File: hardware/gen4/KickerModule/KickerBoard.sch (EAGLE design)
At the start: 106 parts

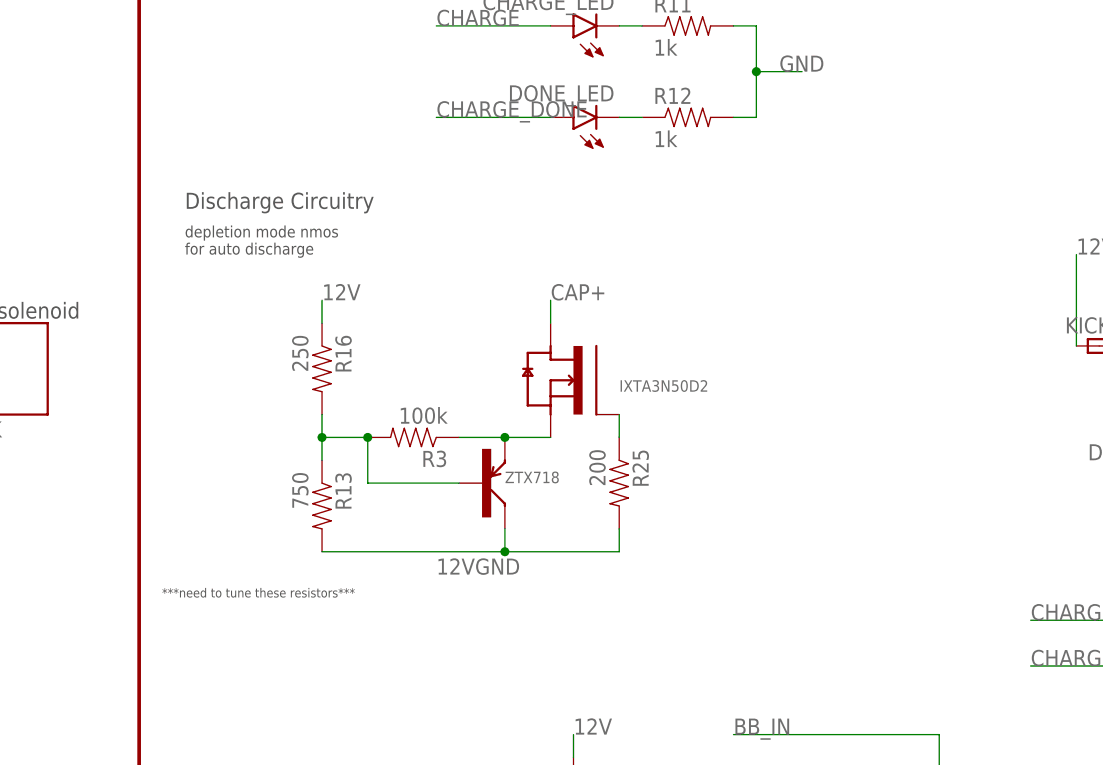
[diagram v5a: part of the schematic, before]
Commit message: discharge circuit improved in schematic
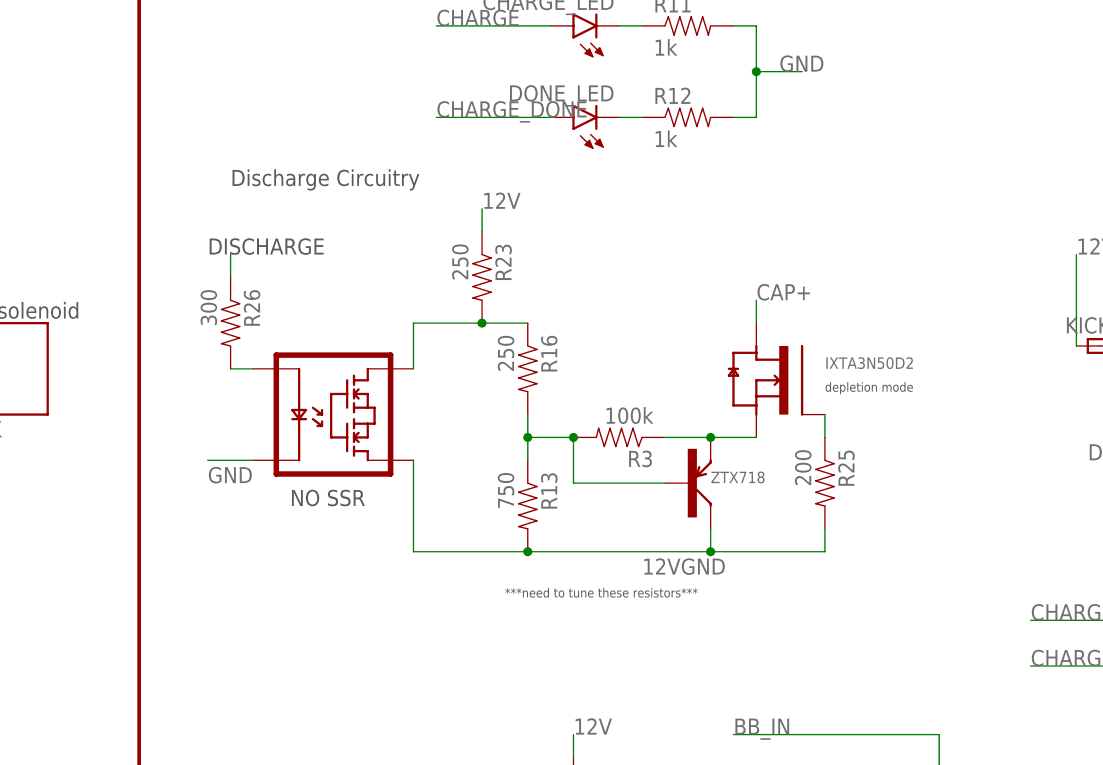
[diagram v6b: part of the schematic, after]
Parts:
- added R23: 250, SparkFun-Passives:RESISTOR0805-RES
- added R26: 300, SparkFun-Passives:RESISTOR0805-RES
- added U$5: VO1400AEFTR, rfc:VO1400AEFTR
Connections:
- new net N$29: R16.1, R23.2, U$5.S1
- new net N$30: R26.2, U$5.LED+
- net 12V: now also R23.1; no longer R16.1
- net 12VGND: now also U$5.S2
- net DISCHARGE: now also R26.1
- net GND: now also U$5.LED-
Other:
- note added: "NO SSR"
- note added: "depletion mode"
- note removed: "depletion mode nmos for auto discharge"
- moved on the sheet: R13, R16, R25, R3
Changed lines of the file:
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@@
 <part name="R16" library="SparkFun-Passives" deviceset="RESISTOR" device="0805-RES" value="250"/>
 <part name="R25" library="SparkFun-Passives" deviceset="RESISTOR" device="0805-RES" value="200"/>
+<part name="U$5" library="rfc" deviceset="VO1400AEFTR" device=""/>
+<part name="R23" library="SparkFun-Passives" deviceset="RESISTOR" device="0805-RES" value="250"/>
+<part name="R26" library="SparkFun-Passives" deviceset="RESISTOR" device="0805-RES" value="300"/>
 </parts>
 <sheets>
@@
 <text x="444.5" y="261.62" size="1.778" layer="97">threshold = 50% of xref</text>
 <text x="698.5" y="370.84" size="1.778" layer="97">same radius, but shorter than old caps</text>
-<text x="513.08" y="350.52" size="1.778" layer="97">Discharge Circuitry</text>
+<text x="518.16" y="353.06" size="1.778" layer="97">Discharge Circuitry</text>
 <text x="538.48" y="241.3" size="1.778" layer="97">capacitor sense circuitry</text>
 <text x="553.72" y="256.54" size="1.778" layer="97" rot="R180">15v -&gt; 3v division
@@
 1.3v drop, 100mA.
 2V / 20 ohm = 100mA</text>
-<text x="513.08" y="345.44" size="1.27" layer="97">depletion mode nmos
-for auto discharge</text>
 <text x="492.252" y="338.328" size="1.778" layer="97">solenoid</text>
 <text x="493.014" y="279.908" size="1.778" layer="97">solenoid</text>
 <text x="386.08" y="231.14" size="1.778" layer="97">DISCHARGE</text>
-<text x="561.34" y="330.2" size="1.27" layer="95">IXTA3N50D2</text>
-<text x="548.64" y="320.04" size="1.27" layer="95">ZTX718</text>
-<text x="510.54" y="307.34" size="1.016" layer="97">***need to tune these resistors***</text>
+<text x="584.2" y="332.74" size="1.27" layer="95">IXTA3N50D2</text>
+<text x="571.5" y="320.04" size="1.27" layer="95">ZTX718</text>
+<text x="548.64" y="307.34" size="1.016" layer="97">***need to tune these resistors***</text>
+<text x="584.2" y="330.2" size="1.016" layer="97">depletion mode</text>
+<text x="515.62" y="345.44" size="1.778" layer="97">DISCHARGE</text>
+<text x="524.764" y="317.5" size="1.778" layer="97">NO SSR</text>
 </plain>
 <instances>
@@
 <attribute name="VALUE" x="613.41" y="332.359" size="1.778" layer="96"/>
 </instance>
-<instance part="U$2" gate="G$1" x="558.8" y="327.66" rot="MR0"/>
-<instance part="U$6" gate="G$1" x="546.1" y="314.96"/>
-<instance part="R3" gate="G$1" x="538.48" y="325.12" rot="R180"/>
-<instance part="R13" gate="G$1" x="528.32" y="317.5" rot="R270"/>
-<instance part="R16" gate="G$1" x="528.32" y="332.74" rot="R270"/>
-<instance part="R25" gate="G$1" x="561.34" y="320.04" rot="R270"/>
+<instance part="U$2" gate="G$1" x="581.66" y="327.66" rot="MR0"/>
+<instance part="U$6" gate="G$1" x="568.96" y="314.96"/>
+<instance part="R3" gate="G$1" x="561.34" y="325.12" rot="R180"/>
+<instance part="R13" gate="G$1" x="551.18" y="317.5" rot="R270"/>
+<instance part="R16" gate="G$1" x="551.18" y="332.74" rot="R270"/>
+<instance part="R25" gate="G$1" x="584.2" y="320.04" rot="R270"/>
+<instance part="U$5" gate="G$1" x="520.7" y="325.12"/>
+<instance part="R23" gate="G$1" x="546.1" y="342.9" rot="R270"/>
+<instance part="R26" gate="G$1" x="518.16" y="337.82" rot="R270"/>
 </instances>
 <busses>
@@
 <junction x="368.3" y="208.28"/>
 <wire x1="368.3" y1="208.28" x2="383.54" y2="208.28" width="0.1524" layer="91"/>
+<label x="515.62" y="320.04" size="1.778" layer="95"/>
+</segment>
+<segment>
+<pinref part="U$5" gate="G$1" pin="LED-"/>
+<wire x1="520.7" y1="322.58" x2="515.62" y2="322.58" width="0.1524" layer="91"/>
 </segment>
 </net>
@@
 <wire x1="482.6" y1="307.34" x2="482.6" y2="302.26" width="0.1524" layer="91"/>
 <label x="482.6" y="302.26" size="1.778" layer="95"/>
-<label x="541.02" y="309.88" size="1.778" layer="95"/>
+<label x="563.88" y="309.88" size="1.778" layer="95"/>
 </segment>
 <segment>
@@
 <pinref part="U$6" gate="G$1" pin="COLLECTOR"/>
 <pinref part="R13" gate="G$1" pin="2"/>
-<wire x1="548.64" y1="314.96" x2="548.64" y2="312.42" width="0.1524" layer="91"/>
-<wire x1="548.64" y1="312.42" x2="528.32" y2="312.42" width="0.1524" layer="91"/>
+<wire x1="571.5" y1="314.96" x2="571.5" y2="312.42" width="0.1524" layer="91"/>
+<wire x1="571.5" y1="312.42" x2="551.18" y2="312.42" width="0.1524" layer="91"/>
 <pinref part="R25" gate="G$1" pin="2"/>
-<wire x1="548.64" y1="312.42" x2="561.34" y2="312.42" width="0.1524" layer="91"/>
-<wire x1="561.34" y1="312.42" x2="561.34" y2="314.96" width="0.1524" layer="91"/>
-<junction x="548.64" y="312.42"/>
+<wire x1="571.5" y1="312.42" x2="584.2" y2="312.42" width="0.1524" layer="91"/>
+<wire x1="584.2" y1="312.42" x2="584.2" y2="314.96" width="0.1524" layer="91"/>
+<junction x="571.5" y="312.42"/>
+<pinref part="U$5" gate="G$1" pin="S2"/>
+<wire x1="538.48" y1="322.58" x2="538.48" y2="312.42" width="0.1524" layer="91"/>
+<wire x1="538.48" y1="312.42" x2="551.18" y2="312.42" width="0.1524" layer="91"/>
+<junction x="551.18" y="312.42"/>
 </segment>
 </net>
@@
 </segment>
 <segment>
-<label x="553.72" y="340.36" size="1.778" layer="95"/>
-<wire x1="553.72" y1="337.82" x2="553.72" y2="340.36" width="0.1524" layer="91"/>
+<label x="576.58" y="340.36" size="1.778" layer="95"/>
+<wire x1="576.58" y1="337.82" x2="576.58" y2="340.36" width="0.1524" layer="91"/>
 <pinref part="U$2" gate="G$1" pin="DRAIN"/>
 </segment>
@@
 <wire x1="612.14" y1="335.28" x2="612.14" y2="345.44" width="0.1524" layer="91"/>
 <label x="612.14" y="345.44" size="1.778" layer="95"/>
-<label x="528.32" y="340.36" size="1.778" layer="95"/>
-</segment>
-<segment>
-<pinref part="R16" gate="G$1" pin="1"/>
-<wire x1="528.32" y1="337.82" x2="528.32" y2="340.36" width="0.1524" layer="91"/>
+<label x="546.1" y="350.52" size="1.778" layer="95"/>
+</segment>
+<segment>
+<pinref part="R23" gate="G$1" pin="1"/>
+<wire x1="546.1" y1="347.98" x2="546.1" y2="350.52" width="0.1524" layer="91"/>
 </segment>
 </net>
@@
 <wire x1="383.54" y1="231.14" x2="393.7" y2="231.14" width="0.1524" layer="91"/>
 <junction x="383.54" y="231.14"/>
+</segment>
+<segment>
+<pinref part="R26" gate="G$1" pin="1"/>
+<wire x1="518.16" y1="342.9" x2="518.16" y2="345.44" width="0.1524" layer="91"/>
 </segment>
 </net>
@@
 <pinref part="U$2" gate="G$1" pin="SOURCE"/>
 <pinref part="U$6" gate="G$1" pin="EMITTER"/>
-<wire x1="553.72" y1="325.12" x2="548.64" y2="325.12" width="0.1524" layer="91"/>
+<wire x1="576.58" y1="325.12" x2="571.5" y2="325.12" width="0.1524" layer="91"/>
 <pinref part="R3" gate="G$1" pin="1"/>
-<wire x1="548.64" y1="325.12" x2="543.56" y2="325.12" width="0.1524" layer="91"/>
-<junction x="548.64" y="325.12"/>
+<wire x1="571.5" y1="325.12" x2="566.42" y2="325.12" width="0.1524" layer="91"/>
+<junction x="571.5" y="325.12"/>
 </segment>
 </net>
@@
 <pinref part="R16" gate="G$1" pin="2"/>
 <pinref part="R13" gate="G$1" pin="1"/>
-<wire x1="528.32" y1="327.66" x2="528.32" y2="325.12" width="0.1524" layer="91"/>
+<wire x1="551.18" y1="327.66" x2="551.18" y2="325.12" width="0.1524" layer="91"/>
 <pinref part="R3" gate="G$1" pin="2"/>
-<wire x1="528.32" y1="325.12" x2="528.32" y2="322.58" width="0.1524" layer="91"/>
-<wire x1="533.4" y1="325.12" x2="528.32" y2="325.12" width="0.1524" layer="91"/>
-<junction x="528.32" y="325.12"/>
+<wire x1="551.18" y1="325.12" x2="551.18" y2="322.58" width="0.1524" layer="91"/>
+<wire x1="556.26" y1="325.12" x2="551.18" y2="325.12" width="0.1524" layer="91"/>
+<junction x="551.18" y="325.12"/>
 <pinref part="U$6" gate="G$1" pin="BASE"/>
-<wire x1="543.56" y1="320.04" x2="533.4" y2="320.04" width="0.1524" layer="91"/>
-<wire x1="533.4" y1="320.04" x2="533.4" y2="325.12" width="0.1524" layer="91"/>
-<junction x="533.4" y="325.12"/>
+<wire x1="566.42" y1="320.04" x2="556.26" y2="320.04" width="0.1524" layer="91"/>
+<wire x1="556.26" y1="320.04" x2="556.26" y2="325.12" width="0.1524" layer="91"/>
+<junction x="556.26" y="325.12"/>
 </segment>
 </net>
@@
 <pinref part="U$2" gate="G$1" pin="GATE"/>
 <pinref part="R25" gate="G$1" pin="1"/>
-<wire x1="561.34" y1="325.12" x2="561.34" y2="327.66" width="0.1524" layer="91"/>
-</segment>
-</net>
+<wire x1="584.2" y1="325.12" x2="584.2" y2="327.66" width="0.1524" layer="91"/>
+</segment>
+</net>
+<net name="N$29" class="0">
+<segment>
+<pinref part="U$5" gate="G$1" pin="S1"/>
+<pinref part="R16" gate="G$1" pin="1"/>
+<wire x1="538.48" y1="332.74" x2="538.48" y2="337.82" width="0.1524" layer="91"/>
+<wire x1="538.48" y1="337.82" x2="546.1" y2="337.82" width="0.1524" layer="91"/>
+<pinref part="R23" gate="G$1" pin="2"/>
+<wire x1="546.1" y1="337.82" x2="551.18" y2="337.82" width="0.1524" layer="91"/>
+<junction x="546.1" y="337.82"/>
+</segment>
+</net>
+<net name="N$30" class="0">
+<segment>
+<pinref part="U$5" gate="G$1" pin="LED+"/>
+<pinref part="R26" gate="G$1" pin="2"/>
+<wire x1="518.16" y1="332.74" x2="520.7" y2="332.74" width="0.1524" layer="91"/>
+</segment>
+</net>

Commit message: main board layout updated
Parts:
- removed POLARITY_PROTECT: BAT60J, diode:BAT60J
- added U$7: 1N4007, rfc:1N4007
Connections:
- removed net BAT+_UNPROTECTED: BATT-1.KL, POLARITY_PROTECT.A
- new net N$36: U$2.DRAIN, U$7.D-
- net BAT+: now also BATT-1.KL; no longer POLARITY_PROTECT.C
- net CAP+: now also U$7.D+; no longer U$2.DRAIN
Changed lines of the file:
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@@
 <part name="BATSENSE_TEST" library="gen3" deviceset="TEST_PT" device=""/>
 <part name="TMP" library="SparkFun-Passives" deviceset="RESISTOR" device="0805-RES" value="0"/>
-<part name="POLARITY_PROTECT" library="diode" deviceset="BAT60J" device=""/>
 <part name="R19" library="SparkFun-Passives" deviceset="RESISTOR" device="0805-RES" value="20"/>
 <part name="C12" library="SparkFun-Capacitors" deviceset="CAP" device="0805" value="4.7uF"/>
@@
 <part name="R23" library="SparkFun-Passives" deviceset="RESISTOR" device="0805-RES" value="250"/>
 <part name="R26" library="SparkFun-Passives" deviceset="RESISTOR" device="0805-RES" value="300"/>
+<part name="U$7" library="rfc" deviceset="1N4007" device=""/>
 </parts>
 <sheets>
@@
 </instance>
 <instance part="TMP" gate="G$1" x="459.74" y="332.74" rot="MR180"/>
-<instance part="POLARITY_PROTECT" gate="G$1" x="365.76" y="360.68" smashed="yes">
-<attribute name="NAME" x="355.854" y="362.585" size="1.778" layer="95"/>
-<attribute name="VALUE" x="363.474" y="357.251" size="1.778" layer="96"/>
-</instance>
 <instance part="R19" gate="G$1" x="589.28" y="264.16" rot="R90"/>
 <instance part="C12" gate="G$1" x="579.12" y="276.86"/>
@@
 <instance part="R23" gate="G$1" x="546.1" y="342.9" rot="R270"/>
 <instance part="R26" gate="G$1" x="518.16" y="337.82" rot="R270"/>
+<instance part="U$7" gate="G$1" x="576.58" y="340.36"/>
 </instances>
 <busses>
@@
 <wire x1="637.54" y1="368.3" x2="637.54" y2="373.38" width="0.1524" layer="91"/>
 <label x="637.54" y="373.38" size="1.778" layer="95"/>
+<label x="576.58" y="345.44" size="1.778" layer="95"/>
 </segment>
 <segment>
@@
 </segment>
 <segment>
-<label x="576.58" y="340.36" size="1.778" layer="95"/>
-<wire x1="576.58" y1="337.82" x2="576.58" y2="340.36" width="0.1524" layer="91"/>
-<pinref part="U$2" gate="G$1" pin="DRAIN"/>
+<pinref part="U$7" gate="G$1" pin="D+"/>
+<wire x1="576.58" y1="342.9" x2="576.58" y2="345.44" width="0.1524" layer="91"/>
 </segment>
 </net>
@@
 </segment>
 </net>
-<net name="BAT+" class="0">
-<segment>
-<pinref part="ON/OFF" gate="G$1" pin="COM"/>
-<wire x1="373.38" y1="360.68" x2="373.38" y2="370.84" width="0.1524" layer="91"/>
-<wire x1="373.38" y1="370.84" x2="396.24" y2="370.84" width="0.1524" layer="91"/>
-<wire x1="396.24" y1="370.84" x2="396.24" y2="365.76" width="0.1524" layer="91"/>
-<pinref part="ON/OFF" gate="G$1" pin="P1"/>
-<wire x1="396.24" y1="365.76" x2="393.7" y2="365.76" width="0.1524" layer="91"/>
-<label x="381" y="370.84" size="1.778" layer="95"/>
-<pinref part="POLARITY_PROTECT" gate="G$1" pin="C"/>
-<wire x1="368.3" y1="360.68" x2="373.38" y2="360.68" width="0.1524" layer="91"/>
-</segment>
-</net>
 <net name="BATSENSE" class="0">
 <segment>
@@
 <pinref part="DRIB_TRAN" gate="G$1" pin="D"/>
 <pinref part="DRIB" gate="G$1" pin="P$2"/>
-</segment>
-</net>
-<net name="BAT+_UNPROTECTED" class="0">
-<segment>
-<pinref part="BATT" gate="-1" pin="KL"/>
-<pinref part="POLARITY_PROTECT" gate="G$1" pin="A"/>
-<wire x1="363.22" y1="360.68" x2="358.14" y2="360.68" width="0.1524" layer="91"/>
 </segment>
 </net>
@@
 </segment>
 </net>
+<net name="N$36" class="0">
+<segment>
+<pinref part="U$2" gate="G$1" pin="DRAIN"/>
+<pinref part="U$7" gate="G$1" pin="D-"/>
+</segment>
+</net>
+<net name="BAT+" class="0">
+<segment>
+<pinref part="BATT" gate="-1" pin="KL"/>
+<pinref part="ON/OFF" gate="G$1" pin="COM"/>
+<wire x1="373.38" y1="360.68" x2="373.38" y2="370.84" width="0.1524" layer="91"/>
+<wire x1="373.38" y1="370.84" x2="396.24" y2="370.84" width="0.1524" layer="91"/>
+<wire x1="396.24" y1="370.84" x2="396.24" y2="365.76" width="0.1524" layer="91"/>
+<pinref part="ON/OFF" gate="G$1" pin="P1"/>
+<wire x1="396.24" y1="365.76" x2="393.7" y2="365.76" width="0.1524" layer="91"/>
+<label x="381" y="370.84" size="1.778" layer="95"/>
+<wire x1="358.14" y1="360.68" x2="373.38" y2="360.68" width="0.1524" layer="91"/>
+</segment>
+</net>

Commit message: values for discharge circuitry for now
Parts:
- R13: value 750 -> 2.5k
- R16: value 250 -> 1k
- R23: value 250 -> 1.5k
- R3: value 100k -> 250k
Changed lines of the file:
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@@
 <setting verticaltext="up"/>
 </settings>
-<grid distance="0.1" unitdist="inch" unit="inch" style="lines" multiple="1" display="yes" altdistance="0.01" altunitdist="inch" altunit="inch"/>
+<grid distance="0.1" unitdist="inch" unit="inch" style="lines" multiple="1" display="no" altdistance="0.01" altunitdist="inch" altunit="inch"/>
 <layers>
 <layer number="1" name="Top" color="4" fill="1" visible="no" active="no"/>
@@
 <part name="U$2" library="rfc" deviceset="IXTA3N50D2" device=""/>
 <part name="U$6" library="rfc" deviceset="ZTX718" device=""/>
-<part name="R3" library="SparkFun-Passives" deviceset="RESISTOR" device="0805-RES" value="100k"/>
-<part name="R13" library="SparkFun-Passives" deviceset="RESISTOR" device="0805-RES" value="750"/>
-<part name="R16" library="SparkFun-Passives" deviceset="RESISTOR" device="0805-RES" value="250"/>
+<part name="R3" library="SparkFun-Passives" deviceset="RESISTOR" device="0805-RES" value="250k"/>
+<part name="R13" library="SparkFun-Passives" deviceset="RESISTOR" device="0805-RES" value="2.5k"/>
+<part name="R16" library="SparkFun-Passives" deviceset="RESISTOR" device="0805-RES" value="1k"/>
 <part name="R25" library="SparkFun-Passives" deviceset="RESISTOR" device="0805-RES" value="200"/>
 <part name="U$5" library="rfc" deviceset="VO1400AEFTR" device=""/>
-<part name="R23" library="SparkFun-Passives" deviceset="RESISTOR" device="0805-RES" value="250"/>
+<part name="R23" library="SparkFun-Passives" deviceset="RESISTOR" device="0805-RES" value="1.5k"/>
 <part name="R26" library="SparkFun-Passives" deviceset="RESISTOR" device="0805-RES" value="300"/>
 <part name="U$7" library="rfc" deviceset="1N4007" device=""/>
